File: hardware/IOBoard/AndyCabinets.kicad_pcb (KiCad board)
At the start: 2 copper layers, 33 x 66.5 mm, 47 parts, among them SW1 Mode_Encoder, SW2 Color_Encoder, U1 74HC14

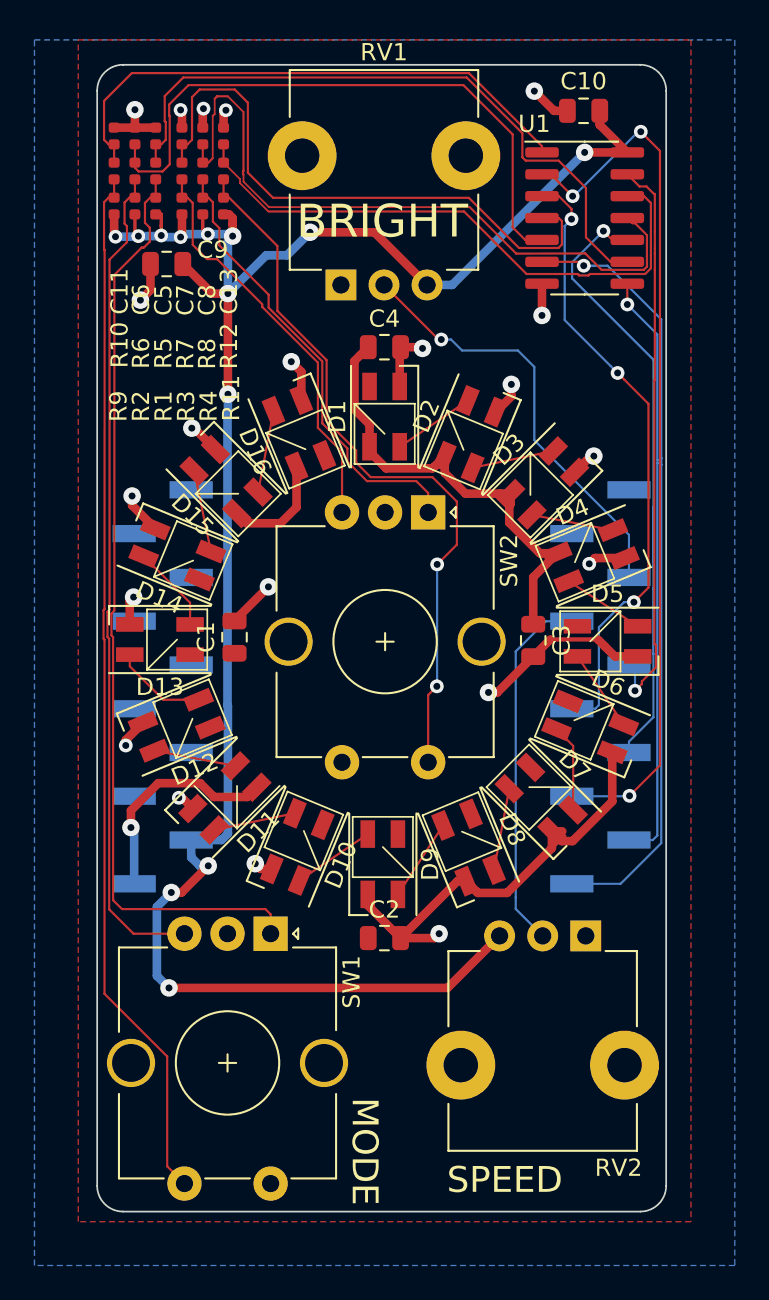
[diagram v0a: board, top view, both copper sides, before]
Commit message: Added faceplate boards
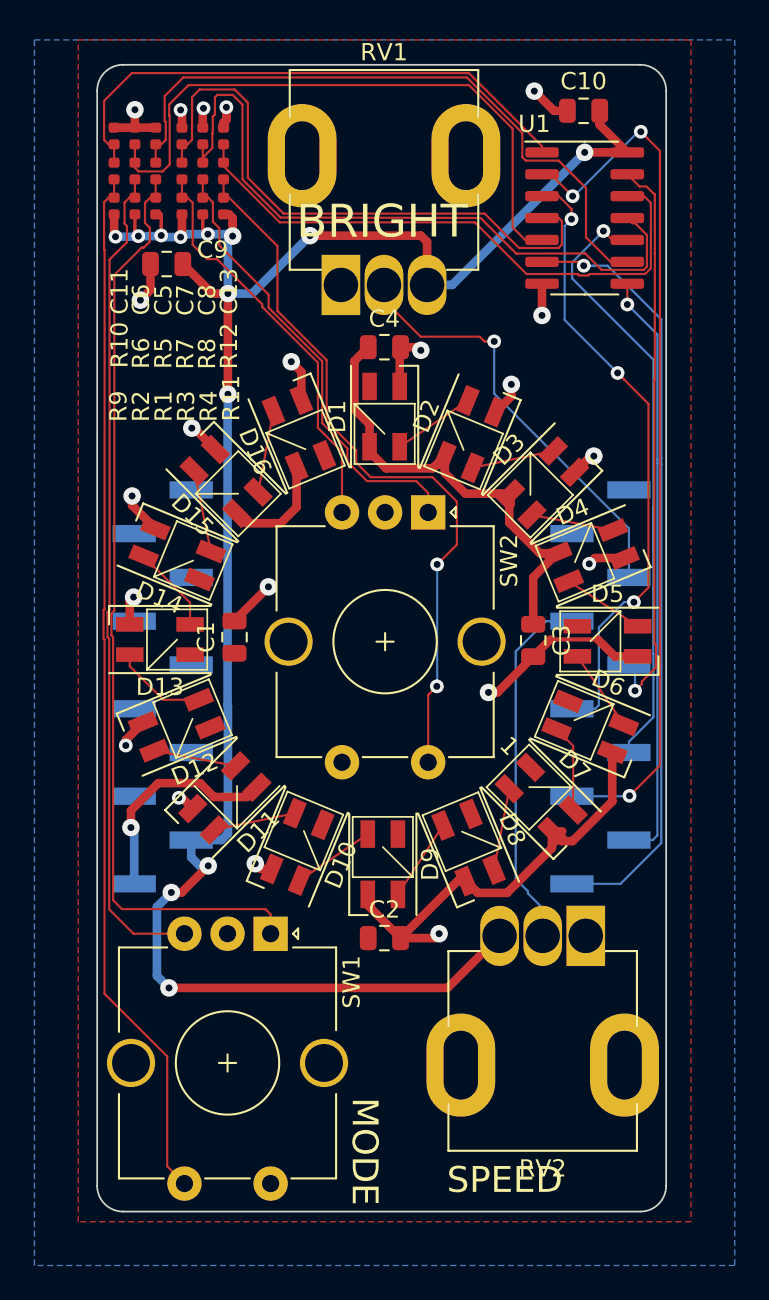
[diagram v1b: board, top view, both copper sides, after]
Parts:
- RV1, RV2: footprint Potentiometer_THT:Potentiometer_TT_P0915N -> YonaFootprints:Potentiometer_TT_P0915N_Flush
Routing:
- net +3V3: track 120.9 -> 122.2 mm
